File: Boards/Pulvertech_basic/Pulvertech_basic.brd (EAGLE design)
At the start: 76.2 x 38.4 mm, 23 parts, among them IC1 786TV, K3 G5LE, Q2 BC548, U2 ATTINY85-20PU

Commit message: update for manufactoring
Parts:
- moved X6 2.89 mm to (72.0, 27.6)
- moved X4 2.74 mm to (72.0, 10.8)
- moved C1 1.64 mm to (59.7, 27.6)
- moved U2 1.64 mm to (25.8, 24.7)
- moved R1 1.36 mm to (36.9, 28.5)
- moved C4 1.36 mm to (24.8, 17.1)
- moved X5 1.10 mm to (4.80, 27.3)
- moved SINAL 0.96 mm to (48.6, 23.1)
- moved D1 0.91 mm to (12.4, 10.2)
- moved C5 0.91 mm to (27.6, 6.35)
- moved K3 0.91 mm to (54.3, 11.4)
- moved R4 0.86 mm to (11.5, 28.5)
- moved RESET 0.86 mm to (40.7, 28.5)
- moved R5 0.68 mm to (16.8, 28.5)
- moved X7 0.68 mm to (5.11, 11.7)
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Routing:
- net GND: track 171.7 -> 185.7 mm
- net VIN: track 144.8 -> 150.5 mm
- net VCC: track 34.2 -> 37.4 mm
- net AUTO_VALVE: track 27.3 -> 29.1 mm
- net VALVE_SIGN: track 5.61 -> 7.03 mm
- net N$31: track 4.45 -> 5.36 mm
- net SENSOR_IND: track 17.8 -> 18.6 mm
- net N$6: track 6.88 -> 7.56 mm
- net N$13: track 15.3 -> 15.9 mm
- net N$1: track 10.7 -> 11.2 mm
- added copper zone on layer 16, net N$7
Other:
- board size 76.2 x 38.4 mm -> 83.5 x 40.5 mm
- board text added: "Aberto"
- board text added: "Auto"
- board text added: "Bateria"
- board text added: "Chave"
- board text added: "Com"
- board text added: "Sensor"
- board text added: "Valvula"
- board text removed: "2018"
- board text removed: "BATERIA"
- board text removed: "CHAVE SELETORA"
- board text removed: "FREE BIRD"
- board text removed: "POWER"
- board text removed: "PULVERTECH LITE"
- board text removed: "SENSOR"
- board text removed: "SINAL"
- board text removed: "VALVULA"

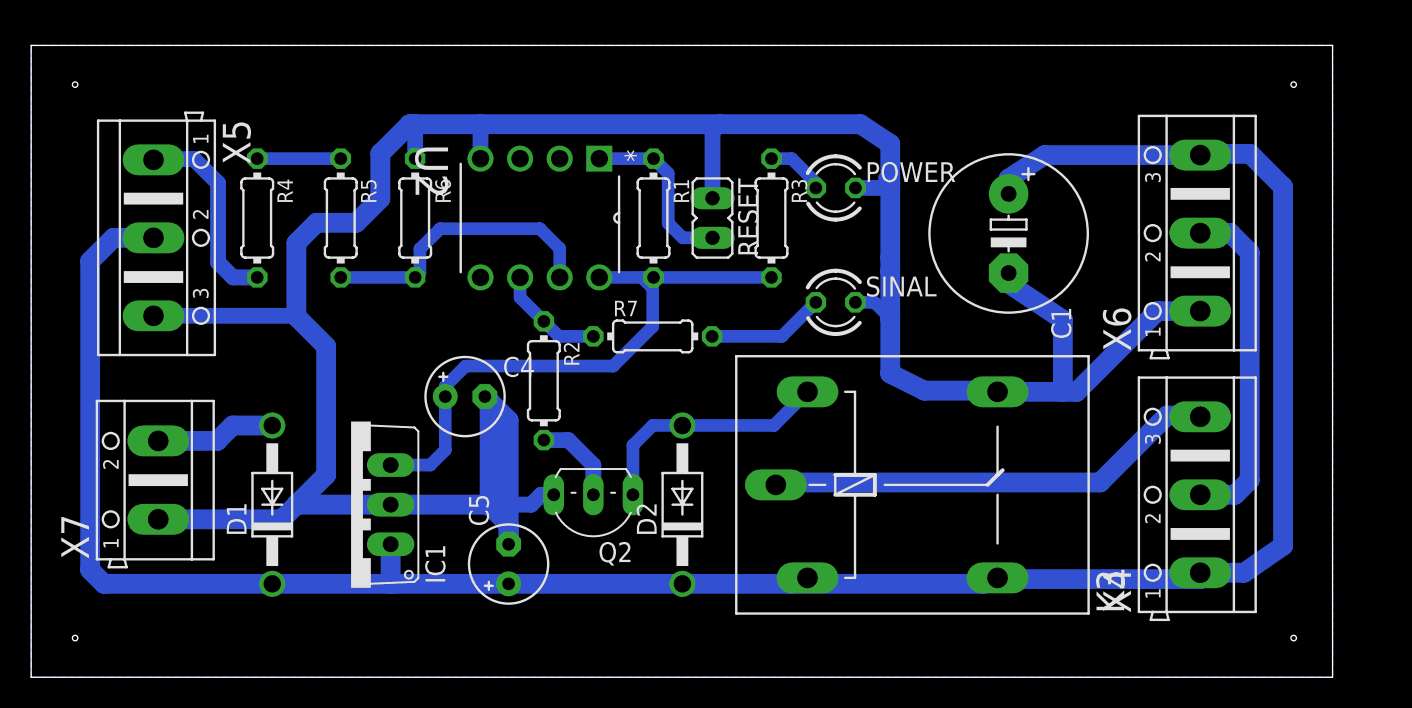
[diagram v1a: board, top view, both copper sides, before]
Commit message: updates for manufactoring
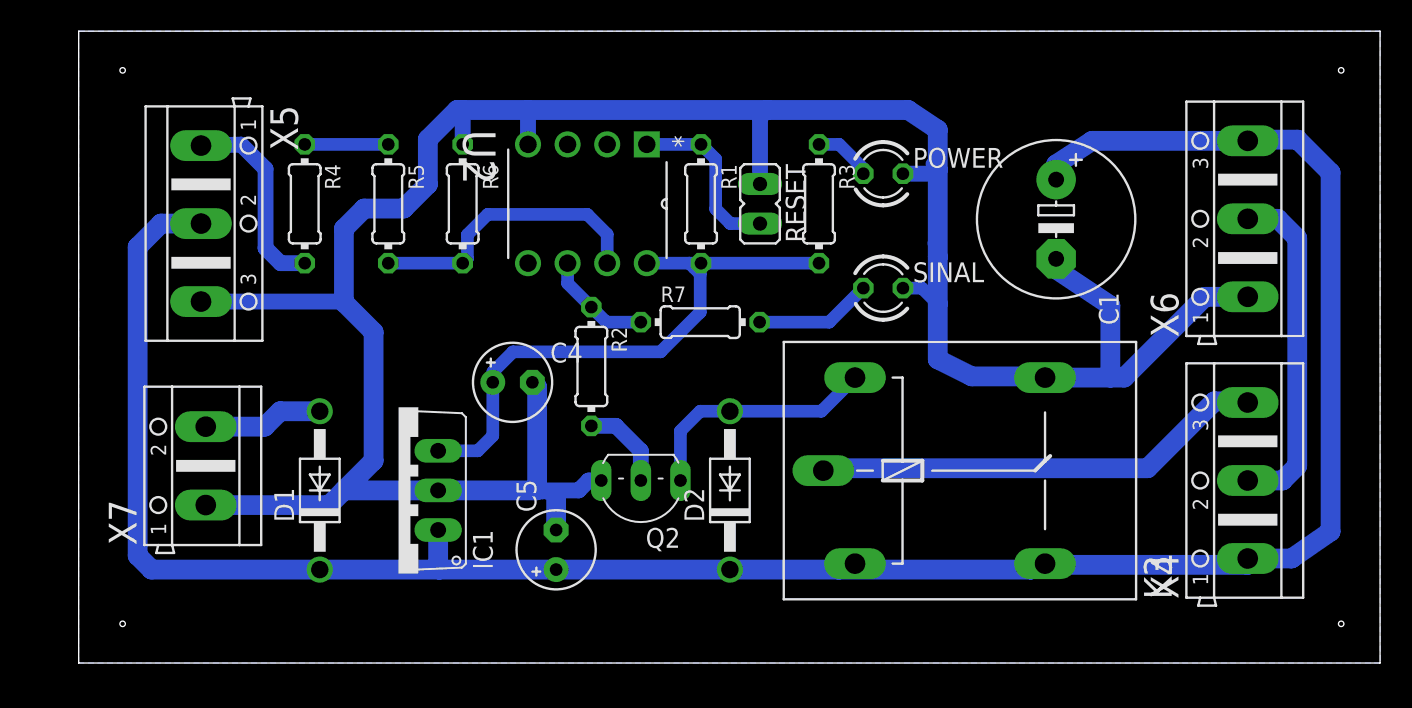
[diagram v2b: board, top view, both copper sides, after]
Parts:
- moved C1 3.18 mm to (62.7, 28.5)
- moved C5 3.18 mm to (30.6, 7.26)
- moved D2 3.18 mm to (41.8, 11.1)
- moved K3 3.18 mm to (57.3, 12.3)
- moved POWER 3.18 mm to (51.6, 31.4)
- moved R2 3.18 mm to (32.9, 19.0)
- moved R7 3.18 mm to (39.9, 21.9)
- moved SINAL 3.18 mm to (51.6, 24.1)
- moved U2 3.18 mm to (28.8, 25.7)
- moved X4 3.18 mm to (75.0, 11.7)
- moved X6 3.18 mm to (75.0, 28.5)
- moved R1 3.18 mm to (39.9, 29.5)
- moved R6 3.18 mm to (24.6, 29.5)
- moved RESET 3.18 mm to (43.7, 29.5)
- moved D1 3.18 mm to (15.5, 11.1)
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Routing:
- net GND: track 185.7 -> 174.7 mm
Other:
- board text added: "PULVERTECH BASIC V1.0 TECHNOAGRI & FREE BIRD"
